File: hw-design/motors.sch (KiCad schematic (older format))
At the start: 12 parts

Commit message: Routing
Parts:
- C16, C17, C18, C19: renamed from C?; footprint (none) -> w_smd_cap:c_0603
- P4, P5: renamed from P?; footprint (none) -> iwasz:stepper-small
- R13, R14, R15, R16: renamed from R?; footprint (none) -> w_smd_resistors:r_0805
- U5, U6: renamed from U?; footprint (none) -> iwasz:drv8835
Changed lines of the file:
@@
 $EndDescr
 $Comp
-L drv8835 U?
+L drv8835 U5
 U 1 1 5725344E
 P 6450 2350
-F 0 "U?" H 6425 2887 60  0000 C CNN
+F 0 "U5" H 6425 2887 60  0000 C CNN
 F 1 "drv8835" H 6425 2781 60  0000 C CNN
-F 2 "" H 6250 2800 60  0000 C CNN
+F 2 "iwasz:drv8835" H 6250 2800 60  0001 C CNN
 F 3 "" H 6250 2800 60  0000 C CNN
 	1    6450 2350
@@
 $EndComp
 $Comp
-L CONN_01X04 P?
+L CONN_01X04 P4
 U 1 1 5725352F
 P 4975 2350
-F 0 "P?" H 5053 2391 50  0000 L CNN
+F 0 "P4" H 5053 2391 50  0000 L CNN
 F 1 "left_motor" H 5053 2300 50  0000 L CNN
-F 2 "" H 4975 2350 50  0000 C CNN
+F 2 "iwasz:stepper-small" H 4975 2350 50  0001 C CNN
 F 3 "" H 4975 2350 50  0000 C CNN
 	1    4975 2350
@@
 $EndComp
 $Comp
-L R R?
+L R R13
 U 1 1 57253CCD
 P 5450 2200
-F 0 "R?" V 5243 2200 50  0000 C CNN
+F 0 "R13" V 5243 2200 50  0000 C CNN
 F 1 "R" V 5334 2200 50  0000 C CNN
-F 2 "" V 5380 2200 50  0000 C CNN
+F 2 "w_smd_resistors:r_0805" V 5380 2200 50  0001 C CNN
 F 3 "" H 5450 2200 50  0000 C CNN
 	1    5450 2200
@@
 $EndComp
 $Comp
-L R R?
+L R R14
 U 1 1 57253D5E
 P 5450 2400
-F 0 "R?" V 5243 2400 50  0000 C CNN
+F 0 "R14" V 5243 2400 50  0000 C CNN
 F 1 "R" V 5334 2400 50  0000 C CNN
-F 2 "" V 5380 2400 50  0000 C CNN
+F 2 "w_smd_resistors:r_0805" V 5380 2400 50  0001 C CNN
 F 3 "" H 5450 2400 50  0000 C CNN
 	1    5450 2400
@@
 	5600 2400 5750 2400
 $Comp
-L GND #PWR?
+L GND #PWR029
 U 1 1 57253FA5
 P 5725 2675
-F 0 "#PWR?" H 5725 2425 50  0001 C CNN
+F 0 "#PWR029" H 5725 2425 50  0001 C CNN
 F 1 "GND" H 5730 2502 50  0000 C CNN
 F 2 "" H 5725 2675 50  0000 C CNN
@@
 	5725 2600 5725 2675
 $Comp
-L +BATT #PWR?
+L +BATT #PWR030
 U 1 1 572546AE
 P 5725 2025
-F 0 "#PWR?" H 5725 1875 50  0001 C CNN
+F 0 "#PWR030" H 5725 1875 50  0001 C CNN
 F 1 "+BATT" H 5740 2198 50  0000 C CNN
 F 2 "" H 5725 2025 50  0000 C CNN
@@
 	5725 2100 5725 2025
 $Comp
-L +3V3 #PWR?
+L +3V3 #PWR031
 U 1 1 572547FA
 P 7175 1775
-F 0 "#PWR?" H 7175 1625 50  0001 C CNN
+F 0 "#PWR031" H 7175 1625 50  0001 C CNN
 F 1 "+3V3" H 7190 1948 50  0000 C CNN
 F 2 "" H 7175 1775 50  0000 C CNN
@@
 Connection ~ 7175 2100
 $Comp
-L C C?
+L C C17
 U 1 1 57254905
 P 7450 2100
-F 0 "C?" V 7198 2100 50  0000 C CNN
+F 0 "C17" V 7198 2100 50  0000 C CNN
 F 1 "100nF" V 7289 2100 50  0000 C CNN
-F 2 "" H 7488 1950 50  0000 C CNN
+F 2 "w_smd_cap:c_0603" H 7488 1950 50  0001 C CNN
 F 3 "" H 7450 2100 50  0000 C CNN
 	1    7450 2100
@@
 $EndComp
 $Comp
-L C C?
+L C C16
 U 1 1 57254998
 P 7450 1875
-F 0 "C?" V 7198 1875 50  0000 C CNN
+F 0 "C16" V 7198 1875 50  0000 C CNN
 F 1 "100nF" V 7289 1875 50  0000 C CNN
-F 2 "" H 7488 1725 50  0000 C CNN
+F 2 "w_smd_cap:c_0603" H 7488 1725 50  0001 C CNN
 F 3 "" H 7450 1875 50  0000 C CNN
 	1    7450 1875
@@
 $EndComp
 $Comp
-L GND #PWR?
+L GND #PWR032
 U 1 1 57254C5E
 P 7750 1775
-F 0 "#PWR?" H 7750 1525 50  0001 C CNN
+F 0 "#PWR032" H 7750 1525 50  0001 C CNN
 F 1 "GND" H 7755 1602 50  0000 C CNN
 F 2 "" H 7750 1775 50  0000 C CNN
@@
 	7100 2600 7400 2600
 $Comp
-L drv8835 U?
+L drv8835 U6
 U 1 1 57256377
 P 6450 4125
-F 0 "U?" H 6425 4662 60  0000 C CNN
+F 0 "U6" H 6425 4662 60  0000 C CNN
 F 1 "drv8835" H 6425 4556 60  0000 C CNN
-F 2 "" H 6250 4575 60  0000 C CNN
+F 2 "iwasz:drv8835" H 6250 4575 60  0001 C CNN
 F 3 "" H 6250 4575 60  0000 C CNN
 	1    6450 4125
@@
 $EndComp
 $Comp
-L CONN_01X04 P?
+L CONN_01X04 P5
 U 1 1 5725637D
 P 4975 4125
-F 0 "P?" H 5053 4166 50  0000 L CNN
+F 0 "P5" H 5053 4166 50  0000 L CNN
 F 1 "right_motor" H 5053 4075 50  0000 L CNN
-F 2 "" H 4975 4125 50  0000 C CNN
+F 2 "iwasz:stepper-small" H 4975 4125 50  0001 C CNN
 F 3 "" H 4975 4125 50  0000 C CNN
 	1    4975 4125
@@
 $EndComp
 $Comp
-L R R?
+L R R15
 U 1 1 57256383
 P 5450 3975
-F 0 "R?" V 5243 3975 50  0000 C CNN
+F 0 "R15" V 5243 3975 50  0000 C CNN
 F 1 "R" V 5334 3975 50  0000 C CNN
-F 2 "" V 5380 3975 50  0000 C CNN
+F 2 "w_smd_resistors:r_0805" V 5380 3975 50  0001 C CNN
 F 3 "" H 5450 3975 50  0000 C CNN
 	1    5450 3975
@@
 $EndComp
 $Comp
-L R R?
+L R R16
 U 1 1 5725638F
 P 5450 4175
-F 0 "R?" V 5243 4175 50  0000 C CNN
+F 0 "R16" V 5243 4175 50  0000 C CNN
 F 1 "R" V 5334 4175 50  0000 C CNN
-F 2 "" V 5380 4175 50  0000 C CNN
+F 2 "w_smd_resistors:r_0805" V 5380 4175 50  0001 C CNN
 F 3 "" H 5450 4175 50  0000 C CNN
 	1    5450 4175
@@
 	5600 4175 5750 4175
 $Comp
-L GND #PWR?
+L GND #PWR033
 U 1 1 572563A3
 P 5725 4450
-F 0 "#PWR?" H 5725 4200 50  0001 C CNN
+F 0 "#PWR033" H 5725 4200 50  0001 C CNN
 F 1 "GND" H 5730 4277 50  0000 C CNN
 F 2 "" H 5725 4450 50  0000 C CNN
@@
 	5725 4375 5725 4450
 $Comp
-L +BATT #PWR?
+L +BATT #PWR034
 U 1 1 572563AB
 P 5725 3800
-F 0 "#PWR?" H 5725 3650 50  0001 C CNN
+F 0 "#PWR034" H 5725 3650 50  0001 C CNN
 F 1 "+BATT" H 5740 3973 50  0000 C CNN
 F 2 "" H 5725 3800 50  0000 C CNN
@@
 	5725 3875 5725 3800
 $Comp
-L +3V3 #PWR?
+L +3V3 #PWR035
 U 1 1 572563B3
 P 7175 3550
-F 0 "#PWR?" H 7175 3400 50  0001 C CNN
+F 0 "#PWR035" H 7175 3400 50  0001 C CNN
 F 1 "+3V3" H 7190 3723 50  0000 C CNN
 F 2 "" H 7175 3550 50  0000 C CNN
@@
 Connection ~ 7175 3875
 $Comp
-L C C?
+L C C19
 U 1 1 572563BD
 P 7450 3875
-F 0 "C?" V 7198 3875 50  0000 C CNN
+F 0 "C19" V 7198 3875 50  0000 C CNN
 F 1 "100nF" V 7289 3875 50  0000 C CNN
-F 2 "" H 7488 3725 50  0000 C CNN
+F 2 "w_smd_cap:c_0603" H 7488 3725 50  0001 C CNN
 F 3 "" H 7450 3875 50  0000 C CNN
 	1    7450 3875
@@
 $EndComp
 $Comp
-L C C?
+L C C18
 U 1 1 572563C3
 P 7450 3650
-F 0 "C?" V 7198 3650 50  0000 C CNN
+F 0 "C18" V 7198 3650 50  0000 C CNN
 F 1 "100nF" V 7289 3650 50  0000 C CNN
-F 2 "" H 7488 3500 50  0000 C CNN
+F 2 "w_smd_cap:c_0603" H 7488 3500 50  0001 C CNN
 F 3 "" H 7450 3650 50  0000 C CNN
 	1    7450 3650
@@
 $EndComp
 $Comp
-L GND #PWR?
+L GND #PWR036
 U 1 1 572563C9
 P 7750 3550
-F 0 "#PWR?" H 7750 3300 50  0001 C CNN
+F 0 "#PWR036" H 7750 3300 50  0001 C CNN
 F 1 "GND" H 7755 3377 50  0000 C CNN
 F 2 "" H 7750 3550 50  0000 C CNN

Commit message: Mounting holes for additional wheels or whatever
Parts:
- added P8, P9: CONN_01X01, symbol CONN_01X01
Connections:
- wire segments 42 -> 44
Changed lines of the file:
@@
 	5600 2400 5750 2400
 $Comp
-L GND #PWR029
+L GND #PWR32
 U 1 1 57253FA5
 P 5725 2675
-F 0 "#PWR029" H 5725 2425 50  0001 C CNN
+F 0 "#PWR32" H 5725 2425 50  0001 C CNN
 F 1 "GND" H 5730 2502 50  0000 C CNN
 F 2 "" H 5725 2675 50  0000 C CNN
@@
 	5725 2600 5725 2675
 $Comp
-L +BATT #PWR030
+L +BATT #PWR31
 U 1 1 572546AE
 P 5725 2025
-F 0 "#PWR030" H 5725 1875 50  0001 C CNN
+F 0 "#PWR31" H 5725 1875 50  0001 C CNN
 F 1 "+BATT" H 5740 2198 50  0000 C CNN
 F 2 "" H 5725 2025 50  0000 C CNN
@@
 	5725 2100 5725 2025
 $Comp
-L +3V3 #PWR031
+L +3V3 #PWR35
 U 1 1 572547FA
 P 7175 1775
-F 0 "#PWR031" H 7175 1625 50  0001 C CNN
+F 0 "#PWR35" H 7175 1625 50  0001 C CNN
 F 1 "+3V3" H 7190 1948 50  0000 C CNN
 F 2 "" H 7175 1775 50  0000 C CNN
@@
 $EndComp
 $Comp
-L GND #PWR032
+L GND #PWR37
 U 1 1 57254C5E
 P 7750 1775
-F 0 "#PWR032" H 7750 1525 50  0001 C CNN
+F 0 "#PWR37" H 7750 1525 50  0001 C CNN
 F 1 "GND" H 7755 1602 50  0000 C CNN
 F 2 "" H 7750 1775 50  0000 C CNN
@@
 	5600 4175 5750 4175
 $Comp
-L GND #PWR033
+L GND #PWR34
 U 1 1 572563A3
 P 5725 4450
-F 0 "#PWR033" H 5725 4200 50  0001 C CNN
+F 0 "#PWR34" H 5725 4200 50  0001 C CNN
 F 1 "GND" H 5730 4277 50  0000 C CNN
 F 2 "" H 5725 4450 50  0000 C CNN
@@
 	5725 4375 5725 4450
 $Comp
-L +BATT #PWR034
+L +BATT #PWR33
 U 1 1 572563AB
 P 5725 3800
-F 0 "#PWR034" H 5725 3650 50  0001 C CNN
+F 0 "#PWR33" H 5725 3650 50  0001 C CNN
 F 1 "+BATT" H 5740 3973 50  0000 C CNN
 F 2 "" H 5725 3800 50  0000 C CNN
@@
 	5725 3875 5725 3800
 $Comp
-L +3V3 #PWR035
+L +3V3 #PWR36
 U 1 1 572563B3
 P 7175 3550
-F 0 "#PWR035" H 7175 3400 50  0001 C CNN
+F 0 "#PWR36" H 7175 3400 50  0001 C CNN
 F 1 "+3V3" H 7190 3723 50  0000 C CNN
 F 2 "" H 7175 3550 50  0000 C CNN
@@
 $EndComp
 $Comp
-L GND #PWR036
+L GND #PWR38
 U 1 1 572563C9
 P 7750 3550
-F 0 "#PWR036" H 7750 3300 50  0001 C CNN
+F 0 "#PWR38" H 7750 3300 50  0001 C CNN
 F 1 "GND" H 7755 3377 50  0000 C CNN
 F 2 "" H 7750 3550 50  0000 C CNN
@@
 Wire Wire Line
 	7100 4375 7400 4375
+$Comp
+L CONN_01X01 P8
+U 1 1 57292D6E
+P 2600 2600
+F 0 "P8" H 2678 2641 50  0000 L CNN
+F 1 "CONN_01X01" H 2678 2550 50  0000 L CNN
+F 2 "" H 2600 2600 50  0000 C CNN
+F 3 "" H 2600 2600 50  0000 C CNN
+	1    2600 2600
+	1    0    0    -1
+$EndComp
+$Comp
+L GND #PWR29
+U 1 1 57293225
+P 2325 2600
+F 0 "#PWR29" H 2325 2350 50  0001 C CNN
+F 1 "GND" H 2330 2427 50  0000 C CNN
+F 2 "" H 2325 2600 50  0000 C CNN
+F 3 "" H 2325 2600 50  0000 C CNN
+	1    2325 2600
+	0    1    1    0
+$EndComp
+Wire Wire Line
+	2325 2600 2400 2600
+$Comp
+L CONN_01X01 P9
+U 1 1 5729335F
+P 2600 2775
+F 0 "P9" H 2678 2816 50  0000 L CNN
+F 1 "CONN_01X01" H 2678 2725 50  0000 L CNN
+F 2 "" H 2600 2775 50  0000 C CNN
+F 3 "" H 2600 2775 50  0000 C CNN
+	1    2600 2775
+	1    0    0    -1
+$EndComp
+$Comp
+L GND #PWR30
+U 1 1 57293365
+P 2325 2775
+F 0 "#PWR30" H 2325 2525 50  0001 C CNN
+F 1 "GND" H 2330 2602 50  0000 C CNN
+F 2 "" H 2325 2775 50  0000 C CNN
+F 3 "" H 2325 2775 50  0000 C CNN
+	1    2325 2775
+	0    1    1    0
+$EndComp
+Wire Wire Line
+	2325 2775 2400 2775
 $EndSCHEMATC

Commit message: patlabor logo
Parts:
- P8, P9: footprint (none) -> Mounting_Holes:MountingHole_2.2mm_M2_ISO7380
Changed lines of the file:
@@
 F 0 "P8" H 2678 2641 50  0000 L CNN
 F 1 "CONN_01X01" H 2678 2550 50  0000 L CNN
-F 2 "" H 2600 2600 50  0000 C CNN
+F 2 "Mounting_Holes:MountingHole_2.2mm_M2_ISO7380" H 2600 2600 50  0001 C CNN
 F 3 "" H 2600 2600 50  0000 C CNN
 	1    2600 2600
@@
 F 0 "P9" H 2678 2816 50  0000 L CNN
 F 1 "CONN_01X01" H 2678 2725 50  0000 L CNN
-F 2 "" H 2600 2775 50  0000 C CNN
+F 2 "Mounting_Holes:MountingHole_2.2mm_M2_ISO7380" H 2600 2775 50  0001 C CNN
 F 3 "" H 2600 2775 50  0000 C CNN
 	1    2600 2775

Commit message: Gerbery 1.1
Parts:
- removed P8, P9: CONN_01X01, Mounting_Holes:MountingHole_2.2mm_M2_ISO7380, symbol CONN_01X01
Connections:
- wire segments 44 -> 42
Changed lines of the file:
@@
 	5600 2400 5750 2400
 $Comp
-L GND #PWR029
+L GND #PWR31
 U 1 1 57253FA5
 P 5725 2675
-F 0 "#PWR029" H 5725 2425 50  0001 C CNN
+F 0 "#PWR31" H 5725 2425 50  0001 C CNN
 F 1 "GND" H 5730 2502 50  0000 C CNN
 F 2 "" H 5725 2675 50  0000 C CNN
@@
 	5725 2600 5725 2675
 $Comp
-L +BATT #PWR030
+L +BATT #PWR30
 U 1 1 572546AE
 P 5725 2025
-F 0 "#PWR030" H 5725 1875 50  0001 C CNN
+F 0 "#PWR30" H 5725 1875 50  0001 C CNN
 F 1 "+BATT" H 5740 2198 50  0000 C CNN
 F 2 "" H 5725 2025 50  0000 C CNN
@@
 	5725 2100 5725 2025
 $Comp
-L +3V3 #PWR031
+L +3V3 #PWR34
 U 1 1 572547FA
 P 7175 1775
-F 0 "#PWR031" H 7175 1625 50  0001 C CNN
+F 0 "#PWR34" H 7175 1625 50  0001 C CNN
 F 1 "+3V3" H 7190 1948 50  0000 C CNN
 F 2 "" H 7175 1775 50  0000 C CNN
@@
 $EndComp
 $Comp
-L GND #PWR032
+L GND #PWR36
 U 1 1 57254C5E
 P 7750 1775
-F 0 "#PWR032" H 7750 1525 50  0001 C CNN
+F 0 "#PWR36" H 7750 1525 50  0001 C CNN
 F 1 "GND" H 7755 1602 50  0000 C CNN
 F 2 "" H 7750 1775 50  0000 C CNN
@@
 	5600 4175 5750 4175
 $Comp
-L GND #PWR033
+L GND #PWR33
 U 1 1 572563A3
 P 5725 4450
-F 0 "#PWR033" H 5725 4200 50  0001 C CNN
+F 0 "#PWR33" H 5725 4200 50  0001 C CNN
 F 1 "GND" H 5730 4277 50  0000 C CNN
 F 2 "" H 5725 4450 50  0000 C CNN
@@
 	5725 4375 5725 4450
 $Comp
-L +BATT #PWR034
+L +BATT #PWR32
 U 1 1 572563AB
 P 5725 3800
-F 0 "#PWR034" H 5725 3650 50  0001 C CNN
+F 0 "#PWR32" H 5725 3650 50  0001 C CNN
 F 1 "+BATT" H 5740 3973 50  0000 C CNN
 F 2 "" H 5725 3800 50  0000 C CNN
@@
 	5725 3875 5725 3800
 $Comp
-L +3V3 #PWR035
+L +3V3 #PWR35
 U 1 1 572563B3
 P 7175 3550
-F 0 "#PWR035" H 7175 3400 50  0001 C CNN
+F 0 "#PWR35" H 7175 3400 50  0001 C CNN
 F 1 "+3V3" H 7190 3723 50  0000 C CNN
 F 2 "" H 7175 3550 50  0000 C CNN
@@
 $EndComp
 $Comp
-L GND #PWR036
+L GND #PWR37
 U 1 1 572563C9
 P 7750 3550
-F 0 "#PWR036" H 7750 3300 50  0001 C CNN
+F 0 "#PWR37" H 7750 3300 50  0001 C CNN
 F 1 "GND" H 7755 3377 50  0000 C CNN
 F 2 "" H 7750 3550 50  0000 C CNN
@@
 Wire Wire Line
 	7100 4375 7400 4375
-$Comp
-L CONN_01X01 P8
-U 1 1 57292D6E
-P 2600 2600
-F 0 "P8" H 2678 2641 50  0000 L CNN
-F 1 "CONN_01X01" H 2678 2550 50  0000 L CNN
-F 2 "Mounting_Holes:MountingHole_2.2mm_M2_ISO7380" H 2600 2600 50  0001 C CNN
-F 3 "" H 2600 2600 50  0000 C CNN
-	1    2600 2600
-	1    0    0    -1
-$EndComp
-$Comp
-L GND #PWR037
-U 1 1 57293225
-P 2325 2600
-F 0 "#PWR037" H 2325 2350 50  0001 C CNN
-F 1 "GND" H 2330 2427 50  0000 C CNN
-F 2 "" H 2325 2600 50  0000 C CNN
-F 3 "" H 2325 2600 50  0000 C CNN
-	1    2325 2600
-	0    1    1    0
-$EndComp
-Wire Wire Line
-	2325 2600 2400 2600
-$Comp
-L CONN_01X01 P9
-U 1 1 5729335F
-P 2600 2775
-F 0 "P9" H 2678 2816 50  0000 L CNN
-F 1 "CONN_01X01" H 2678 2725 50  0000 L CNN
-F 2 "Mounting_Holes:MountingHole_2.2mm_M2_ISO7380" H 2600 2775 50  0001 C CNN
-F 3 "" H 2600 2775 50  0000 C CNN
-	1    2600 2775
-	1    0    0    -1
-$EndComp
-$Comp
-L GND #PWR038
-U 1 1 57293365
-P 2325 2775
-F 0 "#PWR038" H 2325 2525 50  0001 C CNN
-F 1 "GND" H 2330 2602 50  0000 C CNN
-F 2 "" H 2325 2775 50  0000 C CNN
-F 3 "" H 2325 2775 50  0000 C CNN
-	1    2325 2775
-	0    1    1    0
-$EndComp
-Wire Wire Line
-	2325 2775 2400 2775
 $EndSCHEMATC

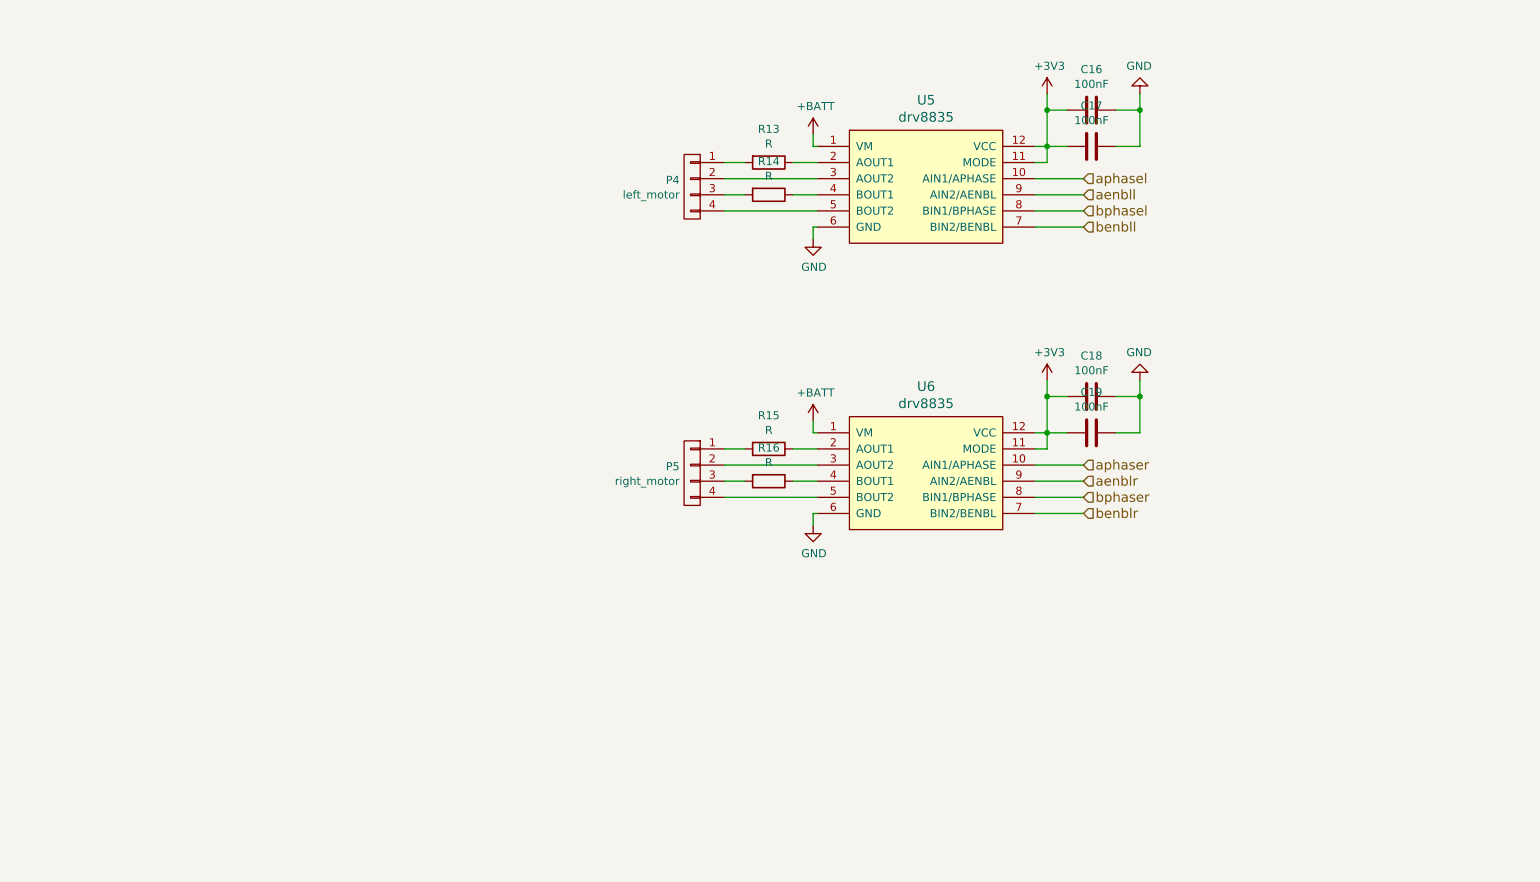
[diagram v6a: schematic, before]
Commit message: 3 boards split
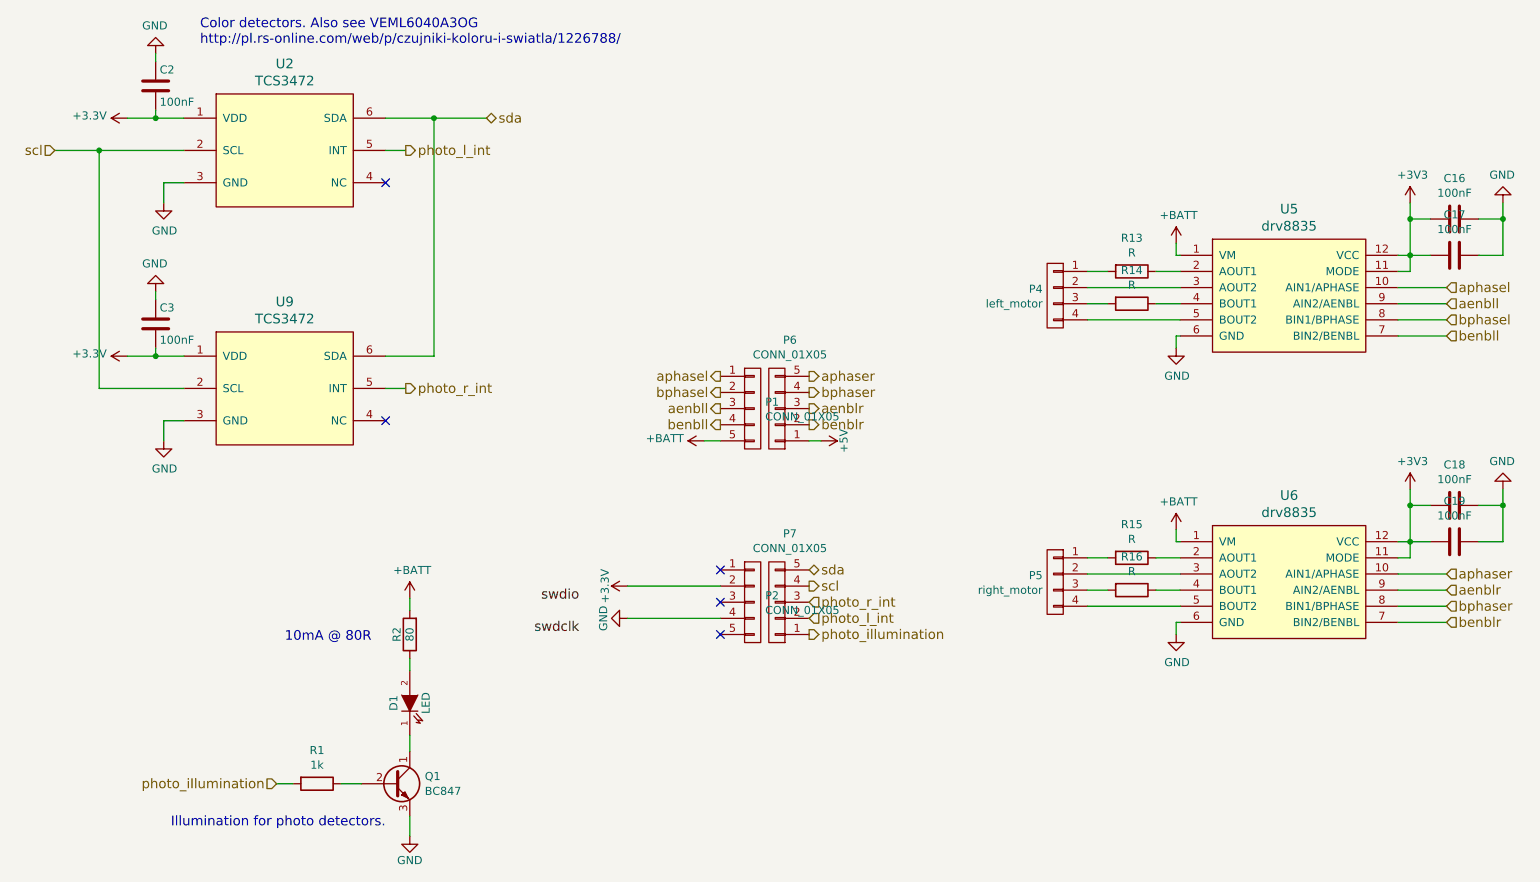
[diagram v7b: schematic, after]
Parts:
- added C2, C3: 100nF, w_smd_cap:c_0603, symbol C
- added D1: LED, LEDs:LED_0805, symbol LED
- added P1, P2, P6, P7: CONN_01X05, w_pin_strip:pin_strip_5, symbol CONN_01X05
- added Q1: BC847, w_smd_trans:sot23, symbol Q_NPN_CBE
- added R1: 1k, w_smd_resistors:r_0402, symbol R
- added R2: 80, w_smd_resistors:r_0603, symbol R
- added U2, U9: TCS3472, iwasz:SC70-6, symbol TCS3472
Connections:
- net +3V3: now also C2.2, C3.2, P2.2 (P2), U2.1 (VDD), U9.1 (VDD)
- net +BATT: now also P1.5 (P5), R2.2
- net GND: now also C2.1, C3.1, P2.4 (P4), Q1.3 (E), U2.3 (GND), U9.3 (GND)
- net aenbll: now also P1.3 (P3)
- net aenblr: now also P6.3 (P3)
- net aphasel: now also P1.1 (P1)
- net aphaser: now also P6.5 (P5)
- net benbll: now also P1.4 (P4)
- net benblr: now also P6.2 (P2)
- net bphasel: now also P1.2 (P2)
- net bphaser: now also P6.4 (P4)
- new net: D1.1 (K), Q1.1 (C)
- new net: D1.2 (A), R2.1
- new net: Q1.2 (B), R1.1
- new net +5V: P6.1 (P1)
- new net photo_illumination: P7.1 (P1), R1.2
- new net photo_l_int: P7.2 (P2), U2.5 (INT)
- new net photo_r_int: P7.3 (P3), U9.5 (INT)
- new net scl: P7.4 (P4), U2.2 (SCL), U9.2 (SCL)
- new net sda: P7.5 (P5), U2.6 (SDA), U9.6 (SDA)
- no-connect marks 0 -> 5
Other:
- note added: "10mA @ 80R"
- note added: "Color detectors. Also see VEML6040A3OG\nhttp://pl.rs-online.com/web/p/czujniki-koloru-i-swiatla/1226788/"
- note added: "Illumination for photo detectors."
- moved on the sheet: C16, C17, C18, C19, P4, P5, R13, R14, R15, R16, U5, U6
